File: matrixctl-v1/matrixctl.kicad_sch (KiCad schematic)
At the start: 24 parts, among them J101 Conn_02x05_Odd_Even, J102 Conn_02x05_Odd_Even, J103 Conn_01x08, J104 USB_B_Micro, U101 IS31FL3738, U102 AP7313-33SR

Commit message: add doc-fields in schematics, add PDFs of schematics
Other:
- company: (none) -> hunz <hunz@mailbox.org>
- title: (none) -> Exposure Notifications LED matrix control

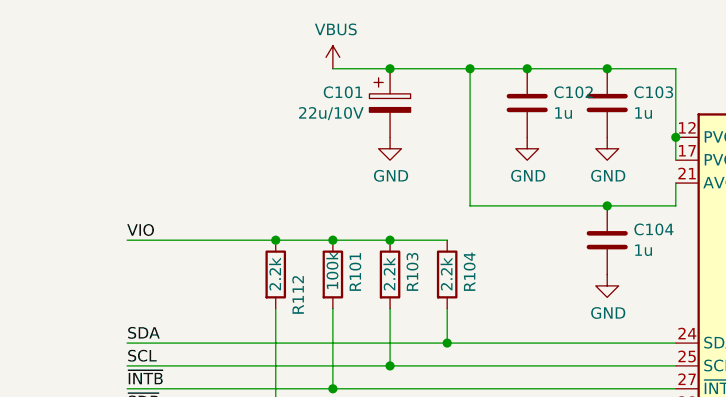
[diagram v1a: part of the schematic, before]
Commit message: 22uF->33uF
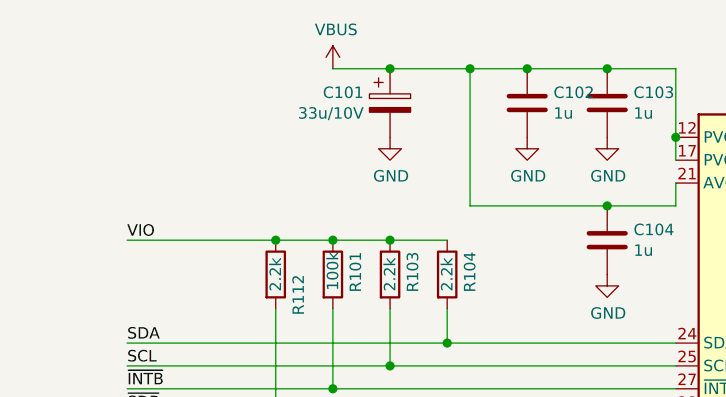
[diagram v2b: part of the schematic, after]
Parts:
- C101: value 22u/10V -> 33u/10V
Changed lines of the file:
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@@
       (effects (font (size 1.27 1.27)) (justify right))
     )
-    (property "Value" "22u/10V" (id 1) (at 92.329 60.839 0)
+    (property "Value" "33u/10V" (id 1) (at 92.329 60.839 0)
       (effects (font (size 1.27 1.27)) (justify right))
     )
@@
     )
     (path "/55938adc-8b31-40b2-bf95-6c3e624a32f2"
-      (reference "C101") (unit 1) (value "22u/10V") (footprint "Capacitor_Tantalum_SMD:CP_EIA-3528-21_Kemet-B")
+      (reference "C101") (unit 1) (value "33u/10V") (footprint "Capacitor_Tantalum_SMD:CP_EIA-3528-21_Kemet-B")
     )
     (path "/ef27c1dd-5522-490f-b6dd-9a9950ca1e1d"
